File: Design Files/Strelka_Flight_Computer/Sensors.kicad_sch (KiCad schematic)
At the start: 0 parts

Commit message: Added sensors
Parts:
- added BT?: MS621FE-FL11E, BAT_MS621FE-FL11E, symbol MS621FE-FL11E:MS621FE-FL11E
- added C? (x2): 100nF, Capacitor_SMD:C_0603_1608Metric, symbol Device:C_Small
- added C?: 10uF, Capacitor_SMD:C_0603_1608Metric, symbol Device:C_Small
- added C?: 4.7u, Capacitor_SMD:C_0603_1608Metric, symbol Device:C_Small
- added C?: 100n, Capacitor_SMD:C_0603_1608Metric, symbol Device:C_Small
- added D?: D_Schottky_Small, symbol Device:D_Schottky_Small
- added D?: LED_BLUE, LED_SMD:LED_0603_1608Metric, symbol Device:LED_Small
- added JP?: UART_Switch, symbol UART_Switch:UART_Switch
- added R? (x2): R_Small, Resistor_SMD:R_0603_1608Metric, symbol Device:R_Small
- added R?: 1k, Resistor_SMD:R_0603_1608Metric, symbol Device:R_Small
- added U?: MS561101BA03-50, Local_footprints:MS561101BA03-50, symbol MS561101BA03-50:MS561101BA03-50
- added U?: L80-M39, Local_footprints:L80-M39, symbol L2_board-rescue:L80-M39-L80-M39
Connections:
- new net: D?.1 (K), R?.2
- new net: R?.1, R?.1, U?.6 (1PPS)
- new net: JP?.2 (TX1), U?.2 (TXD1)
- new net: JP?.4 (RX2), U?.1 (RXD1)
- new net GND: BT?.-, C?.2, C?.2, C?.2, C?.2, C?.2, D?.1 (K), U?.12 (GND), U?.3 (GND), U?.3 (GND), U?.4 (SCB), U?.5 (SCB)
- new net GPS_PPS: R?.2
- new net RXD2_GPS: JP?.3 (TX1)
- new net SCL: U?.8 (SCLK)
- new net SDA: U?.7 (SDI/SDA)
- new net TXD2_GPS: JP?.1 (RX1)
- new net VDD: C?.1, C?.1, C?.1, D?.2 (A), U?.1 (VDD), U?.10 (RESET), U?.2 (PS), U?.4 (VCC)
- new net V_BKCP: BT?.+ (r~), C?.1, C?.1, R?.1, U?.5 (V_BCKP)
- no-connect marks 0 -> 4
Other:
- note added: "ADD MICRO COIN CELL"
- note added: "Barometer"
- note added: "GPS - L80 M39"
- note added: "Schottky should have voltage drop no greater than 3v"

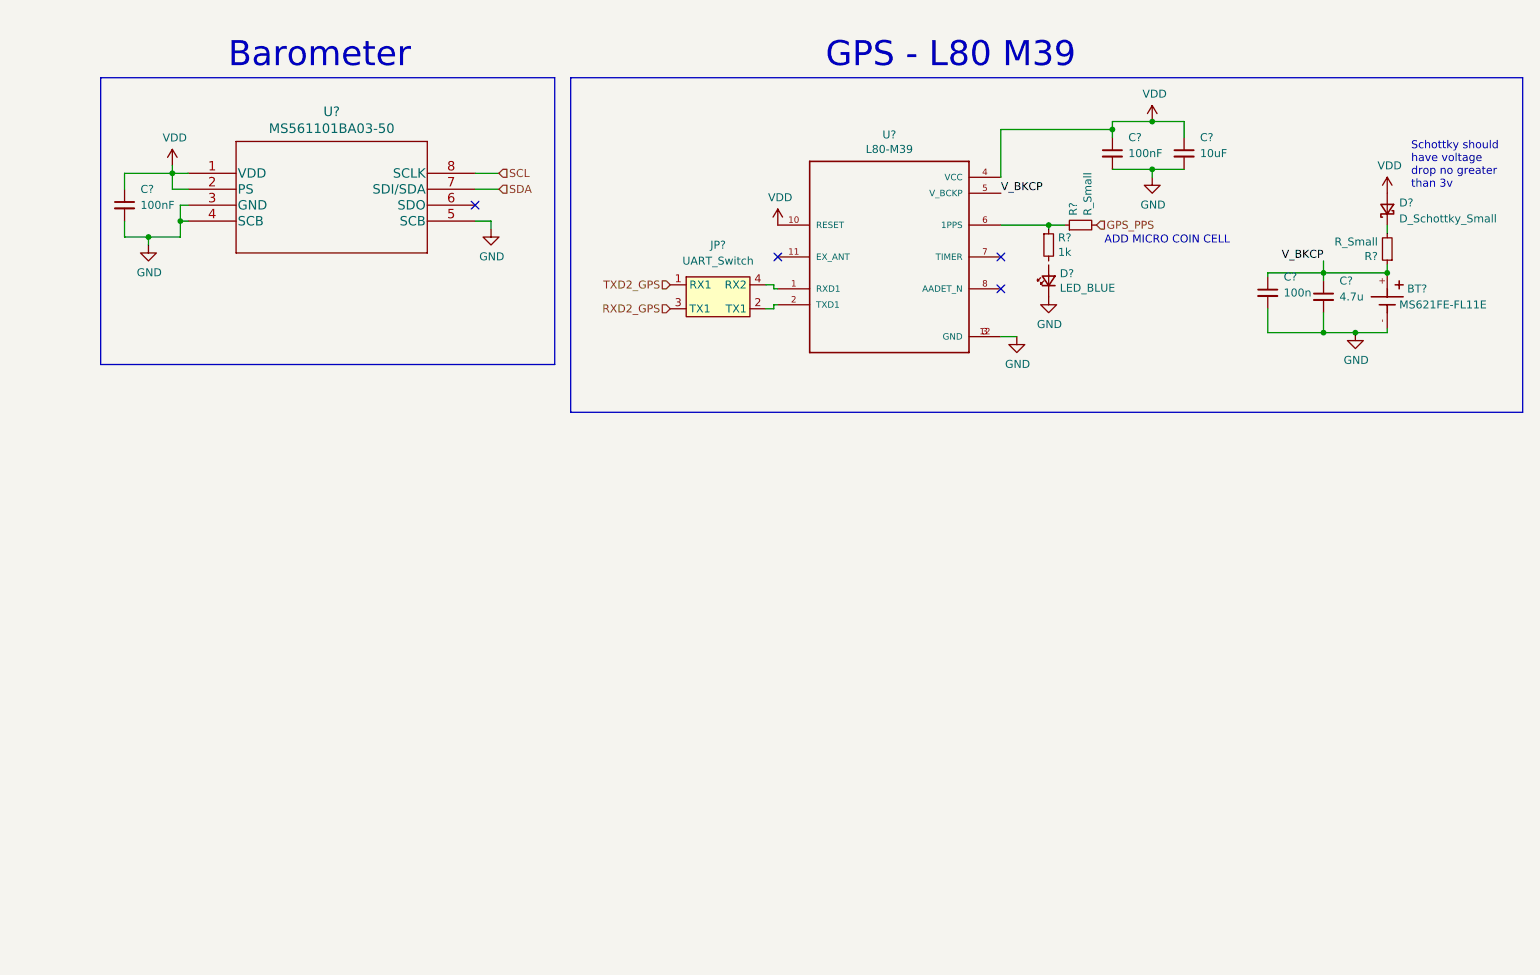
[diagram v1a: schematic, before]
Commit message: Added BMX055
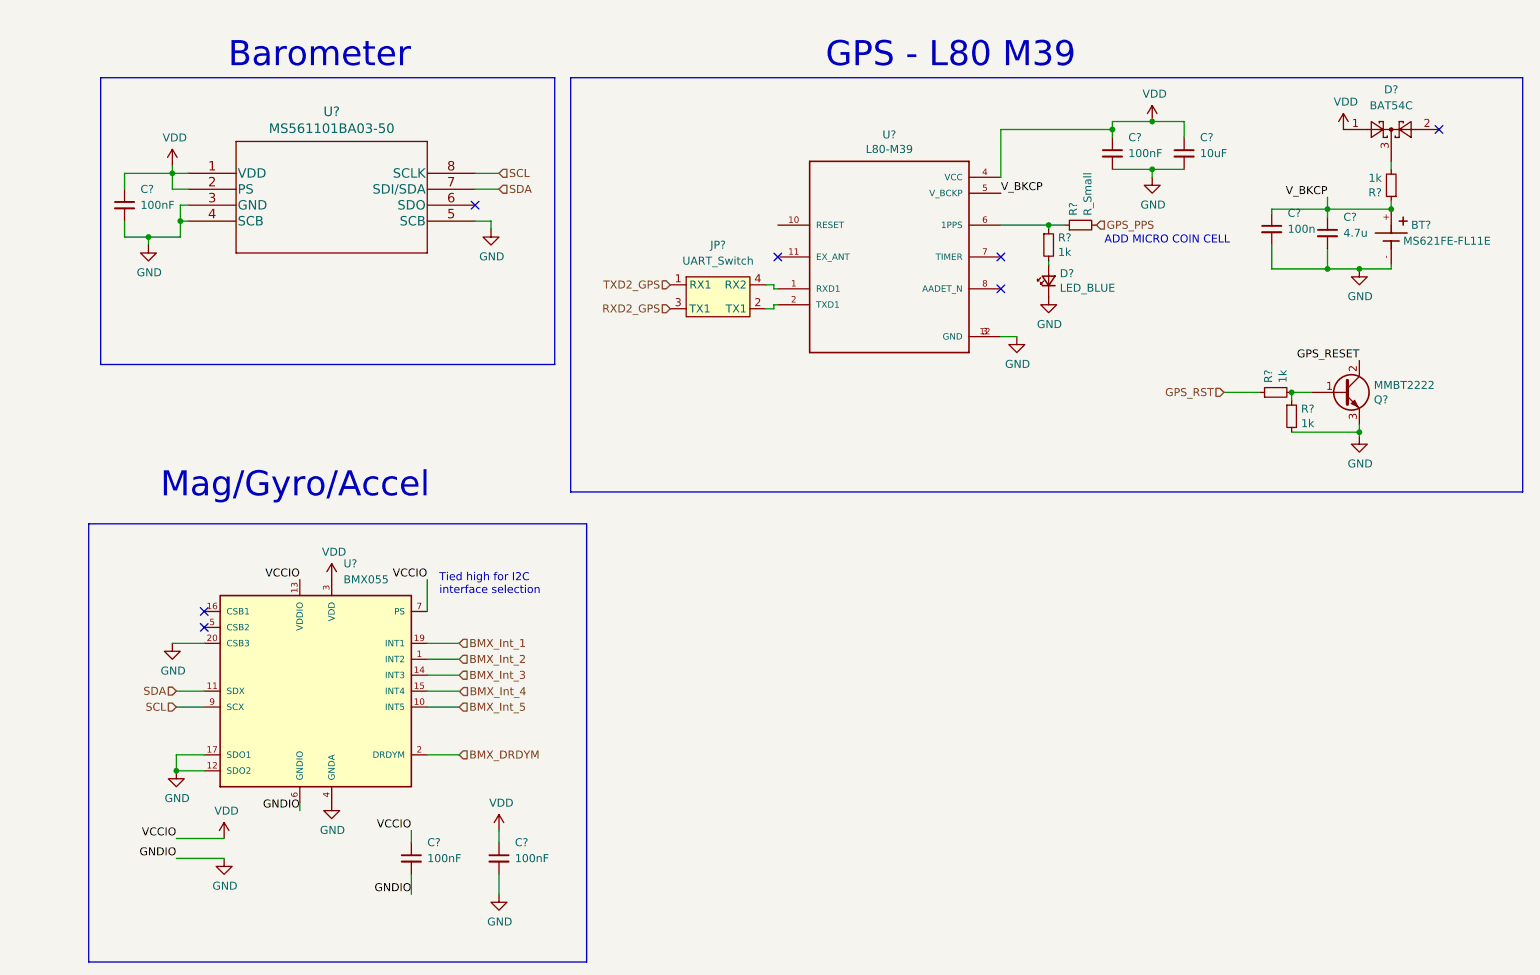
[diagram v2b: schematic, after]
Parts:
- removed D?: D_Schottky_Small, symbol Device:D_Schottky_Small
- added C? (x2): 100nF, Capacitor_SMD:C_0603_1608Metric, symbol Device:C_Small
- added D?: BAT54C, Package_TO_SOT_SMD:SOT-23, symbol Diode:BAT54C
- added Q?: MMBT2222, Package_TO_SOT_SMD:SOT-23, symbol Device:Q_NPN_BCE
- added R? (x2): 1k, Resistor_SMD:R_0603_1608Metric, symbol Device:R_Small
- added U?: BMX055, Footprints:BMX055, symbol BMX055:BMX055
- R?: value R_Small -> 1k
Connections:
- net GND: now also C?.2, C?.2, Q?.3 (E), R?.2, U?.12 (SDO2), U?.17 (SDO1), U?.20 (CSB3), U?.4 (GNDA), U?.6 (GNDIO)
- net SCL: now also U?.9 (SCX)
- net SDA: now also U?.11 (SDX)
- net VDD: now also C?.1, C?.1, D?.1, U?.13 (VDDIO), U?.3 (VDD), U?.7 (PS); no longer U?.10 (RESET)
- net at R?.2: now also D?.3
- net at D?.2 (A): now also R?.2
- new net: Q?.1 (B), R?.1, R?.2
- new net BMX_DRDYM: U?.2 (DRDYM)
- new net BMX_Int_1: U?.19 (INT1)
- new net BMX_Int_2: U?.1 (INT2)
- new net BMX_Int_3: U?.14 (INT3)
- new net BMX_Int_5: U?.10 (INT5)
- new net GPS_RESET: Q?.2 (C)
- new net GPS_RST: R?.1
- no-connect marks 4 -> 7
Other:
- note added: "Mag/Gyro/Accel"
- note added: "Tied high for I2C interface selection"
- note removed: "Schottky should have voltage drop no greater than 3v"
- moved on the sheet: BT?, C?, R?

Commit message: Working SPICE sim for ematch continuity circuit
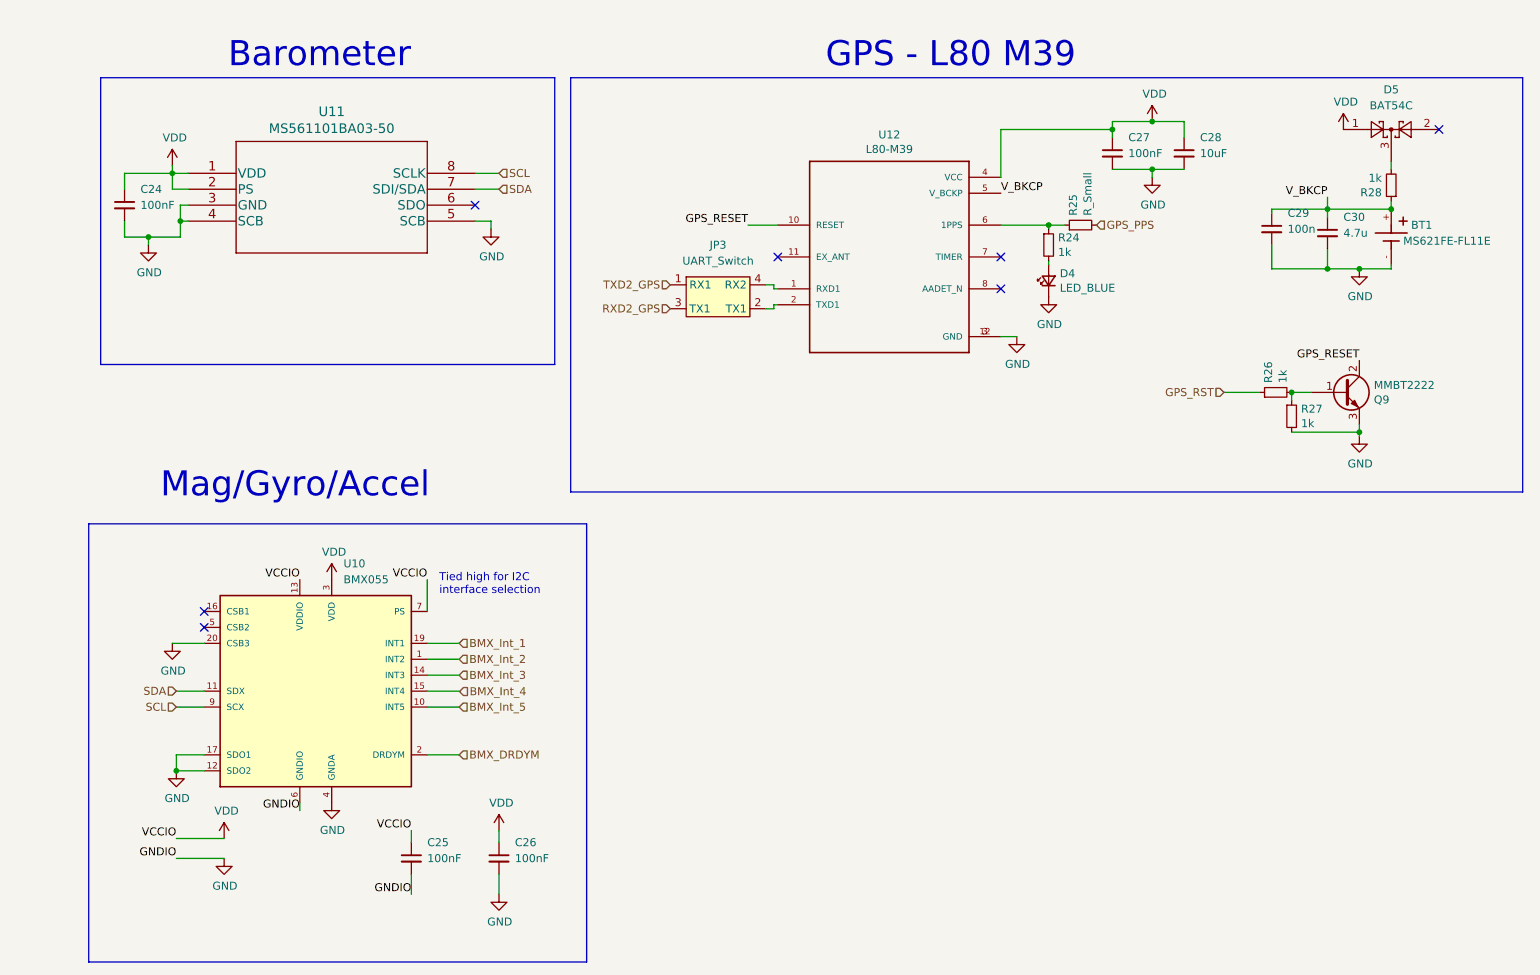
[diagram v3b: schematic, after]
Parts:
- gave numbers to parts that had none: 20
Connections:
- net GPS_RESET: now also U12.10 (RESET)
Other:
- note removed: "ADD MICRO COIN CELL"

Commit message: Added power board, almost finished Strelka schematic
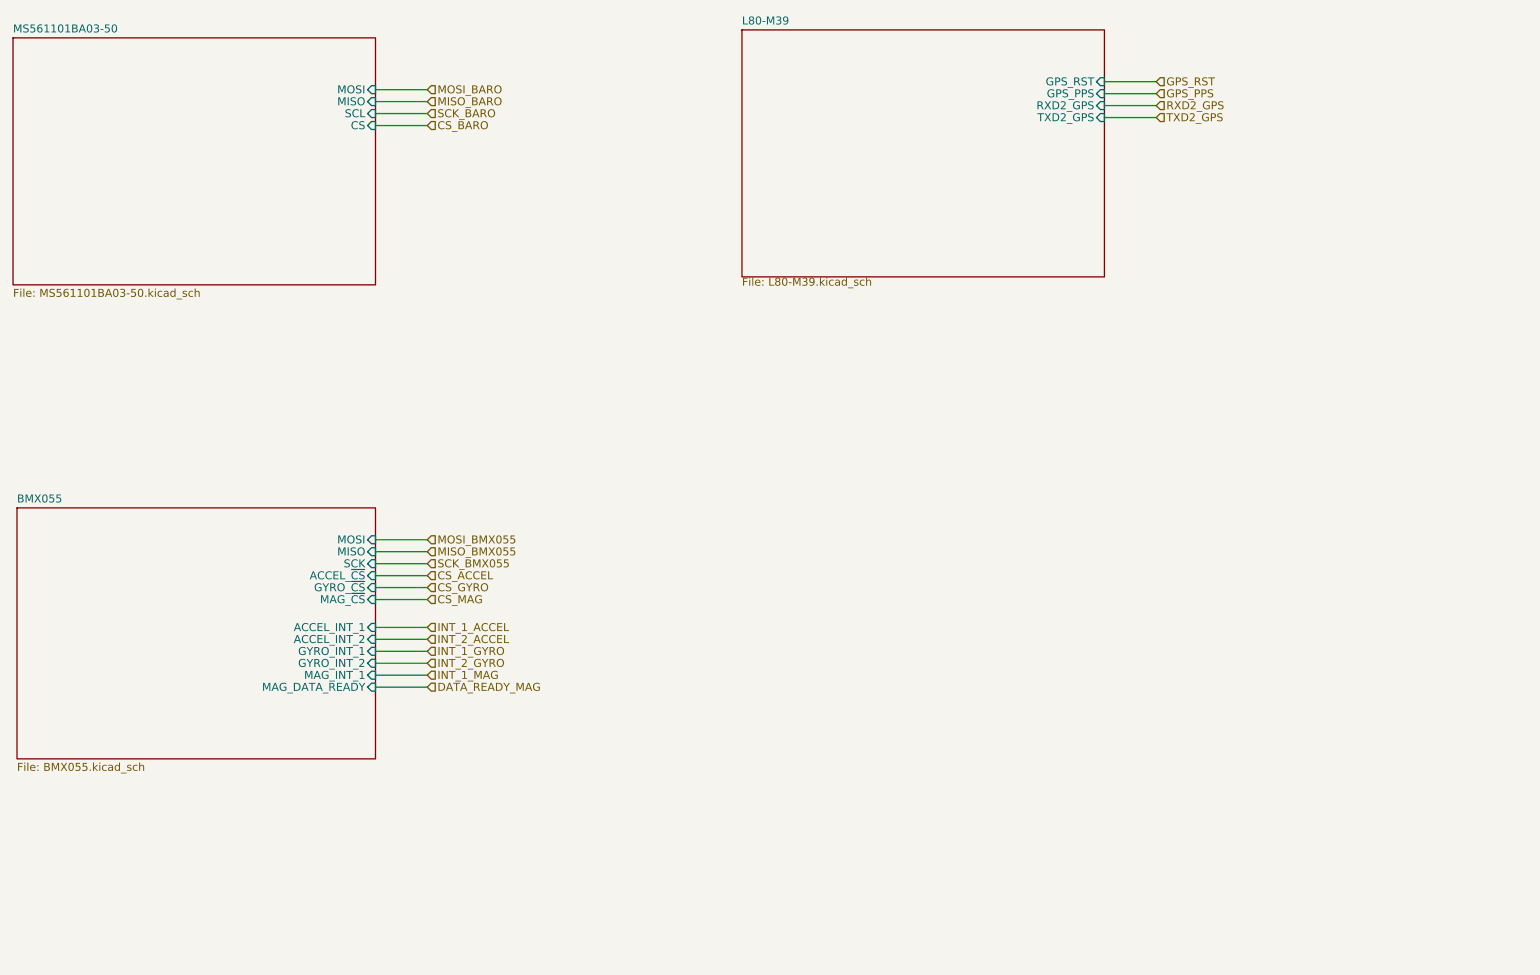
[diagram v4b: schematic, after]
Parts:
- removed BT1: MS621FE-FL11E, BAT_MS621FE-FL11E, symbol MS621FE-FL11E:MS621FE-FL11E
- removed C24, C25, C26, C27: 100nF, Capacitor_SMD:C_0603_1608Metric, symbol Device:C_Small
- removed C28: 10uF, Capacitor_SMD:C_0603_1608Metric, symbol Device:C_Small
- removed C29: 100n, Capacitor_SMD:C_0603_1608Metric, symbol Device:C_Small
- removed C30: 4.7u, Capacitor_SMD:C_0603_1608Metric, symbol Device:C_Small
- removed D4: LED_BLUE, LED_SMD:LED_0603_1608Metric, symbol Device:LED_Small
- removed D5: BAT54C, Package_TO_SOT_SMD:SOT-23, symbol Diode:BAT54C
- removed JP3: UART_Switch, symbol UART_Switch:UART_Switch
- removed Q9: MMBT2222, Package_TO_SOT_SMD:SOT-23, symbol Device:Q_NPN_BCE
- removed R24, R26, R27, R28: 1k, Resistor_SMD:R_0603_1608Metric, symbol Device:R_Small
- removed R25: R_Small, Resistor_SMD:R_0603_1608Metric, symbol Device:R_Small
- removed U10: BMX055, Footprints:BMX055, symbol BMX055:BMX055
- removed U11: MS561101BA03-50, Local_footprints:MS561101BA03-50, symbol MS561101BA03-50:MS561101BA03-50
- removed U12: L80-M39, Local_footprints:L80-M39, symbol L2_board-rescue:L80-M39-L80-M39
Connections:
- no-connect marks 7 -> 0
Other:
- added sheet BMX055 (BMX055.kicad_sch)
- added sheet L80-M39 (L80-M39.kicad_sch)
- added sheet MS561101BA03-50 (MS561101BA03-50.kicad_sch)
- note removed: "Barometer"
- note removed: "GPS - L80 M39"
- note removed: "Mag/Gyro/Accel"
- note removed: "Tied high for I2C interface selection"
